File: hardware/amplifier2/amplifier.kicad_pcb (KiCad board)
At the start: 2 copper layers, 50 x 50 mm, 67 parts, among them IC1 AD8331, IC2 ISL55210, J1 0, P1 5V, P2 3V3, P3 Interface, T1 BALUN, T2 BALUN, U1 MCP4706/16/26, X1 IN_AD, X2 OUT_ISL_B, X3 OUT_AD_B, X4 OUT_AD, X5 IN_ISL, X6 OUT_ISL

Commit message: rerouting nearly done; added remaining footprints
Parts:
- added C26: 82p, Capacitors_SMD:C_0603, F.Cu at (54.4, 168.4)
- added C27: 100u, Capacitors_SMD:C_0603, F.Cu at (234.7, 165.5)
- added C28: 10n, Capacitors_SMD:C_0603, F.Cu at (228.0, 166.8)
- added C29: 180p, Capacitors_SMD:C_0603, F.Cu at (62.8, 166.5)
- added C30: 180p, Capacitors_SMD:C_0603, F.Cu at (70.8, 154.6)
- added C31: 180p, Capacitors_SMD:C_0603, F.Cu at (53.8, 152.0)
- added C32: 100n, Capacitors_SMD:C_0603, F.Cu at (98.8, 168.5)
- added C33: 82p, Capacitors_SMD:C_0603, F.Cu at (51.5, 159.7)
- added C34: 100n, Capacitors_SMD:C_0603, F.Cu at (95.6, 169.1)
- added C35: 100n, Capacitors_SMD:C_0603, F.Cu at (89.2, 157.9)
- added C36: 100n, Capacitors_SMD:C_0603, F.Cu at (81.7, 156.7)
- added C37: 100n, Capacitors_SMD:C_0603, F.Cu at (84.5, 164.7)
- added C38: 100n, Capacitors_SMD:C_0603, F.Cu at (96.6, 148.4)
- added C39: 100n, Capacitors_SMD:C_0603, F.Cu at (96.6, 149.9)
- added C40: 22p, Capacitors_SMD:C_0603, F.Cu at (94.4, 149.2)
- added C41: 10p, Capacitors_SMD:C_0603, F.Cu at (87.1, 152.2)
- added C42: TBD, Capacitors_SMD:C_0603, F.Cu at (110.7, 174.3)
- added C43: 100n, Capacitors_SMD:C_0603, F.Cu at (92.0, 155.2)
- added C44: 2u2, Capacitors_SMD:C_0603, F.Cu at (90.7, 159.3)
- added C45: 1u, Capacitors_SMD:C_0603, F.Cu at (84.7, 153.0)
- added C46: 100n, Capacitors_SMD:C_0402, F.Cu at (84.3, 156.7)
- added C47: 2u2, Capacitors_SMD:C_0603, F.Cu at (84.0, 155.2)
- added C48: 1u, Capacitors_SMD:C_0603, F.Cu at (83.2, 153.0)
- added D1: LED, LEDs:LED_0603, F.Cu at (53.2, 180.6)
- added D2: LED, LEDs:LED_0603, F.Cu at (53.2, 178.9)
- added IC4: NC7SVU04, SDRfootprints:SOT353, F.Cu at (94.9, 165.3)
- added IC5: LTC2252, Housings_DFN_QFN:QFN-32-1EP_5x5mm_Pitch0.5mm, F.Cu at (84.5, 160.4)
- added JP1: DE0_nano_GPIO-1, Pin_Headers:Pin_Header_Angled_2x20, F.Cu at (108.6, 178.4)
- added L10: 307n, SDRfootprints:Coil_132-XXSM_L_, F.Cu at (56.7, 154.0)
- added L11: 390n, SDRfootprints:1008, F.Cu at (91.2, 147.8)
- added L12: 390n, SDRfootprints:1008, F.Cu at (91.2, 150.4)
- added L7: 307n, SDRfootprints:Coil_132-XXSM_L_, F.Cu at (51.4, 166.4)
- added L8: 380n, SDRfootprints:Coil_132-XXSM_L_, F.Cu at (62.1, 162.8)
- added L9: 380n, SDRfootprints:Coil_132-XXSM_L_, F.Cu at (67.4, 150.4)
- added P4: VGA - LNA, Connect:bornier4, F.Cu at (62.7, 107.3)
- added P5: LNA - SDR, Connect:bornier4, F.Cu at (113.0, 142.5)
- added R19: 10k, Resistors_SMD:R_0603, F.Cu at (98.8, 160.2)
- added R20: 10k, Resistors_SMD:R_0603, F.Cu at (97.3, 158.4)
- added R21: 23k2, Resistors_SMD:R_0603, F.Cu at (240.3, 165.6)
- added R22: 13k3, Resistors_SMD:R_0603, F.Cu at (247.8, 163.1)
- added R23: 470, Resistors_SMD:R_0603, F.Cu at (56.0, 180.6)
- added R24: 470, Resistors_SMD:R_0603, F.Cu at (56.0, 178.9)
- added R25: 10k, Resistors_SMD:R_0603, F.Cu at (108.2, 173.5)
- added R26: 3k9, Resistors_SMD:R_0603, F.Cu at (87.1, 153.8)
- added R27: 100, Resistors_SMD:R_0603, F.Cu at (91.3, 153.0)
- added R28: 100, Resistors_SMD:R_0603, F.Cu at (89.6, 153.0)
- added R29: 10k, Resistors_SMD:R_0603, F.Cu at (91.6, 164.2)
- added R30: 22k, Resistors_SMD:R_0603, F.Cu at (91.6, 162.6)
- added R31: 22R, Resistors_SMD:R_0603, F.Cu at (86.3, 155.9)
- added R32: 0R, Resistors_SMD:R_0603, F.Cu at (89.6, 155.9)
- added R33: 22R, Resistors_SMD:R_0603, F.Cu at (88.0, 155.9)
- added R34: 0R, Resistors_SMD:R_0603, F.Cu at (91.0, 160.9)
- added R35: TBD, Resistors_SMD:R_0603, F.Cu at (101.4, 154.7)
- added R36: TBD, Resistors_SMD:R_0603, F.Cu at (104.0, 154.7)
- added R37: TBD, Resistors_SMD:R_0603, F.Cu at (83.8, 130.4)
- added R38: TBD, Resistors_SMD:R_0603, F.Cu at (82.0, 130.4)
- added RP1: R_PACK8, SDRfootprints:2406, F.Cu at (83.7, 166.9)
- added RP2: R_PACK8, SDRfootprints:2406, F.Cu at (90.8, 166.9)
- added SW1: SW_PUSH, Buttons_Switches_SMD:SW_SPST_PTS645, F.Cu at (115.6, 177.5)
- added T3: BALUN, SDRfootprints:CX2041NLT, F.Cu at (102.7, 159.6)
- added T4: BALUN, SDRfootprints:CX2041NLT, F.Cu at (83.0, 125.9)
- added W4: CLCK EXT, Measurement_Points:Test_Point_Keystone_5005-5009_Compact, F.Cu at (158.6, 182.3)
- added X7: OUT_AD, SDRfootprints:1-1337543-0, F.Cu at (44.1, 117.5)
- added Y1: FVXO-HC53BR, SDRfootprints:OSC_631-1265-1-ND, F.Cu at (99.6, 162.9)
- P1: footprint Pin_Headers:Pin_Header_Angled_1x02 -> Connect:bornier2
- P2: value 3V3 -> UART; footprint Pin_Headers:Pin_Header_Angled_1x02 -> Connectors_Molex:Molex_PicoBlade_53398-0471_04x1.25mm_Straight
- P3: value Interface -> DAC Interface
- X2: value OUT_ISL_B -> IN_FILTER
- X3: value OUT_AD_B -> OUT_FILTER
- X4: value OUT_AD -> IN_ADC
- moved P1 184.8 mm to (255.3, 168.0)
- moved P2 183.8 mm to (44.2, 181.9), turned to 0 degrees
- moved C13 138.6 mm to (223.0, 152.2)
- moved C15 138.6 mm to (229.5, 152.3)
- moved C17 138.6 mm to (235.6, 152.2)
- moved C20 138.6 mm to (242.3, 152.2)
- moved L3 138.6 mm to (226.3, 150.7)
- moved L4 138.6 mm to (238.9, 150.7)
- moved X3 126.9 mm to (44.1, 155.8), turned to 90 degrees
- moved X2 125.1 mm to (44.1, 171.8)
- moved T2 96.1 mm to (48.9, 116.3), turned to 270 degrees
- moved L5 92.2 mm to (89.0, 137.9), turned to 0 degrees
- moved R7 90.0 mm to (52.9, 120.7), turned to 0 degrees
- moved R9 89.4 mm to (91.3, 137.4), turned to 90 degrees
- moved R11 89.4 mm to (86.4, 134.6), turned to 270 degrees
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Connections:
- P2 pad 1: GNDA -> +3V3
- P2 pad 2: +3V3 -> /RX
- R17 pad 1: /OUT2+ -> /OUT2-
- R18 pad 1: /OUT2- -> /OUT2+
- X2 pad 1: Net-(T1-Pad1) -> Net-(C26-Pad1)
- X3 pad 1: Net-(T2-Pad1) -> Net-(C33-Pad1)
- X4 pad 1: /OUT2+ -> Net-(T3-Pad1)
- X4 pad 2: /OUT2- -> GNDA
- X5 pad 1: /IN2+ -> Net-(T4-Pad1)
- X5 pad 2: /IN2- -> GNDA
- X6 pad 1: /OUT1+ -> Net-(T1-Pad1)
- X6 pad 2: /OUT1- -> GNDA
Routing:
- net /SW1: track 0.00 -> 27.7 mm
- net /IN3-: track 0.00 -> 23.6 mm
- net /CLK: track 0.00 -> 22.3 mm
- net /RX: track 0.00 -> 21.6 mm
- net /TX: track 0.00 -> 21.1 mm
- net /IN3+: track 0.00 -> 20.8 mm, vias 0 -> 1
- net /D12: track 0.00 -> 18.9 mm
- net /OUT2-: track 0.01 -> 17.7 mm
- net /D11: track 0.00 -> 16.1 mm
- net /HILO: track 15.9 -> 0.00 mm
- net /OUT2+: track 0.00 -> 15.2 mm, vias 0 -> 1
- net /D0: track 0.00 -> 15.0 mm
- net /D9: track 0.00 -> 14.6 mm
- net Net-(C41-Pad1): track 0.00 -> 14.5 mm
- net /D1: track 0.00 -> 14.3 mm
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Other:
- board outline removed

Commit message: last state; minor changes still to do; powersupply missing; outline missing
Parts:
- removed W4: CLCK EXT, Measurement_Points:Test_Point_Keystone_5005-5009_Compact
- moved P3 47.3 mm to (135.2, 146.7)
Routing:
- net /HILO: track 0.00 -> 97.0 mm, vias 0 -> 1
- net /SDA: track 8.34 -> 97.5 mm, vias 0 -> 1
- net /SCL: track 10.4 -> 90.6 mm, vias 0 -> 1
- net /OUT1-: track 6.86 -> 26.1 mm
- net /OUT1+: track 3.85 -> 22.5 mm
- net (no net): track 12.3 -> 2.47 mm, vias 4 -> 3
- net Net-(T1-Pad1): track 4.05 -> 8.11 mm
- net +3V3: track 15.8 -> 19.6 mm
- net +3.3VADC: track 7.86 -> 7.05 mm

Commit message: all routing but PSU done; maybe schema needs nicer annotations
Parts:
- removed P3: DAC Interface, Pin_Headers:Pin_Header_Angled_1x03
- P1: footprint Connect:bornier2 -> SDRfootprints:ED365-2
- P4, P5: footprint Connect:bornier4 -> SDRfootprints:ED365-4
- moved P1 183.7 mm to (82.0, 107.3), turned to 180 degrees
- moved R22 172.4 mm to (79.1, 127.8)
- moved R21 162.6 mm to (82.2, 127.8)
- moved C27 160.4 mm to (77.2, 135.2)
- moved C15 157.7 mm to (72.2, 141.8), turned to 0 degrees
- moved C20 154.8 mm to (88.0, 139.6), turned to 180 degrees
- moved C17 153.0 mm to (82.9, 141.5), turned to 90 degrees
- moved L3 153.0 mm to (73.8, 138.7), turned to 180 degrees
- moved L4 152.6 mm to (86.5, 143.0), turned to 0 degrees
- moved C13 151.7 mm to (72.3, 135.3), turned to 180 degrees
- moved C28 149.4 mm to (82.9, 131.5)
- moved L5 15.1 mm to (103.1, 132.6)
- moved C23 15.1 mm to (102.8, 125.1)
- moved C25 15.1 mm to (108.2, 125.5)
- moved IC2 15.1 mm to (102.6, 127.2)
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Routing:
- net +5V: track 3.30 -> 97.5 mm, vias 0 -> 1
- net +3V3: track 19.6 -> 103.0 mm, vias 0 -> 4
- net +3.3VADC: track 7.05 -> 87.4 mm, vias 0 -> 5
- net /IN2-: track 7.76 -> 51.9 mm, vias 0 -> 1
- net /IN2+: track 5.71 -> 45.8 mm, vias 0 -> 1
- net +5VA: track 35.8 -> 55.9 mm, vias 2 -> 6
- net /OUT1+: track 22.5 -> 12.8 mm
- net /OUT1-: track 26.1 -> 18.8 mm
- net /IN3-: track 23.6 -> 30.3 mm
- net /IN3+: track 20.8 -> 27.3 mm
- net GNDA: track 116.4 -> 111.2 mm, vias 71 -> 60
- net /OUT2+: track 15.2 -> 18.7 mm
- net Net-(T3-Pad1): track 10.8 -> 13.7 mm
- net (no net): track 2.47 -> 0.00 mm, vias 3 -> 0
- net Net-(C30-Pad1): track 9.93 -> 12.4 mm
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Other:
- board outline added: 92 x 82 mm
- board text added: "ADC"
- board text added: "LGA"
- board text added: "LP"
- board text added: "PSU"
- board text added: "VGA"

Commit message: Updated and placed LDO, added wip bom. routing is wip
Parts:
- added IC3: LP38798, Housings_DFN_QFN:DFN-12-1EP_4x4mm_Pitch0.5mm, F.Cu at (82.9, 135.6)
- C27: footprint Capacitors_SMD:C_0603 -> Capacitors_SMD:C_1206
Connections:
- IC2 pad 10: Net-(IC2-Pad10) -> (no net)
- IC2 pad 11: Net-(IC2-Pad11) -> (no net)
- IC4 pad 1: Net-(IC4-Pad1) -> (no net)
- IC5 pad 9: Net-(IC5-Pad9) -> (no net)
- JP1 pad 15: Net-(JP1-Pad15) -> (no net)
- JP1 pad 18: Net-(JP1-Pad18) -> (no net)
- JP1 pad 2: Net-(JP1-Pad2) -> (no net)
- JP1 pad 20: Net-(JP1-Pad20) -> (no net)
- JP1 pad 25: Net-(JP1-Pad25) -> (no net)
- JP1 pad 27: Net-(JP1-Pad27) -> (no net)
- JP1 pad 3: Net-(JP1-Pad3) -> (no net)
- JP1 pad 32: Net-(JP1-Pad32) -> (no net)
- JP1 pad 33: Net-(JP1-Pad33) -> (no net)
- JP1 pad 34: Net-(JP1-Pad34) -> (no net)
- JP1 pad 35: Net-(JP1-Pad35) -> (no net)
- JP1 pad 8: Net-(JP1-Pad8) -> (no net)
- Y1 pad 5: Net-(Y1-Pad5) -> (no net)

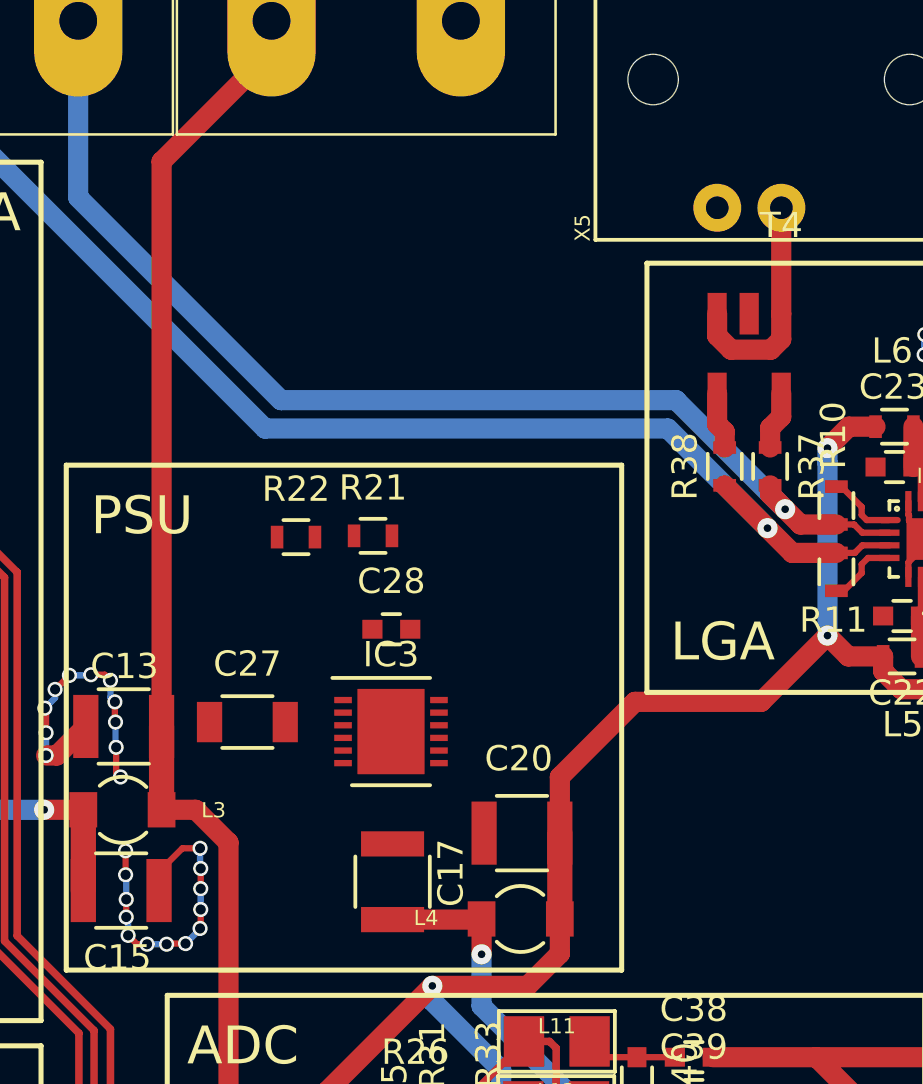
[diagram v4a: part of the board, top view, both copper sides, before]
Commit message: Routed LDO, updated LED resistors, added resistor part numbers
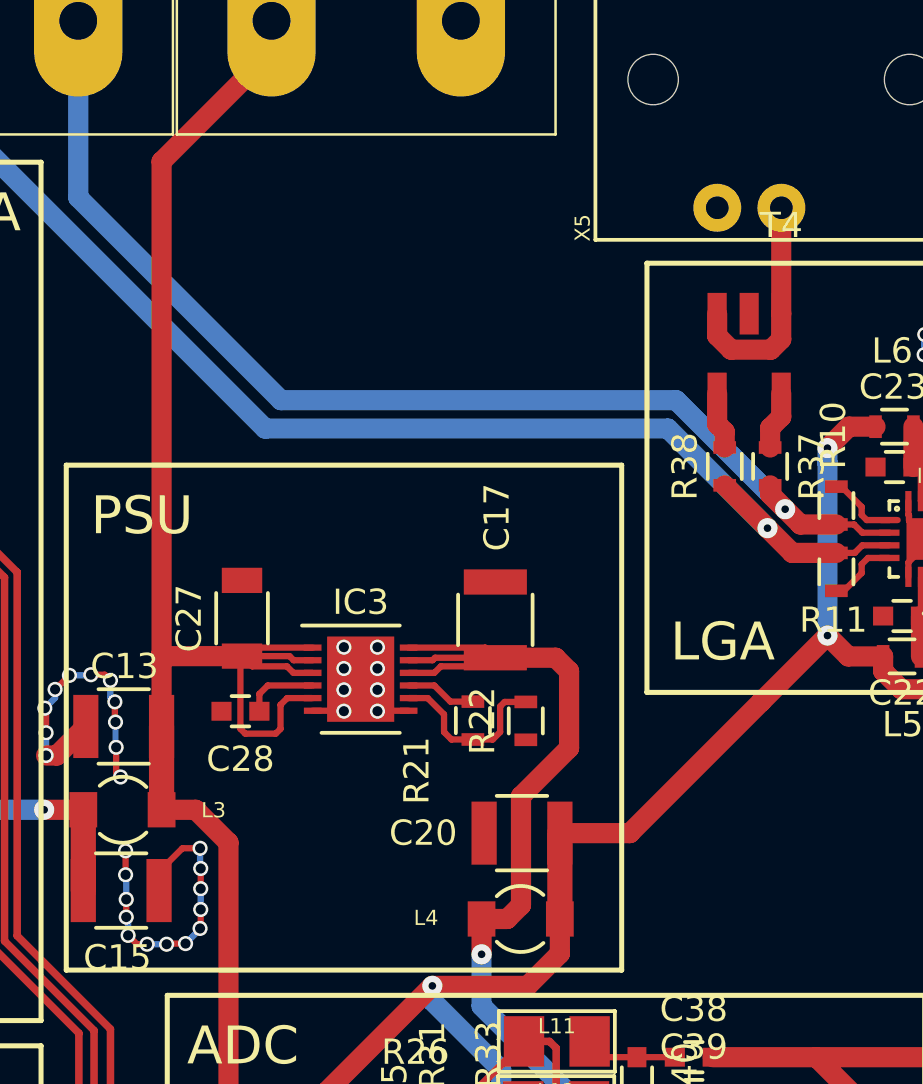
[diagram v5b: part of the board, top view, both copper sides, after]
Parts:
- moved R22 11.7 mm to (88.2, 135.1), turned to 90 degrees
- moved C17 11.1 mm to (87.0, 131.1)
- moved R21 8.32 mm to (86.1, 135.1), turned to 90 degrees
- moved C28 6.80 mm to (76.9, 134.7), turned to 180 degrees
- moved C27 4.12 mm to (77.0, 131.1), turned to 90 degrees
- moved IC3 2.40 mm to (81.7, 133.5)
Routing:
- net +3V3: track 103.0 -> 125.3 mm
- net +5V: track 97.5 -> 116.8 mm
- net Net-(IC3-Pad8): track 0.00 -> 6.94 mm
- net Net-(C28-Pad1): track 0.00 -> 2.94 mm
- net Net-(IC3-Pad9): track 0.00 -> 2.81 mm
- net GNDA: track 111.2 -> 113.7 mm, vias 60 -> 68
- net +3.3VADC: track 87.4 -> 86.1 mm

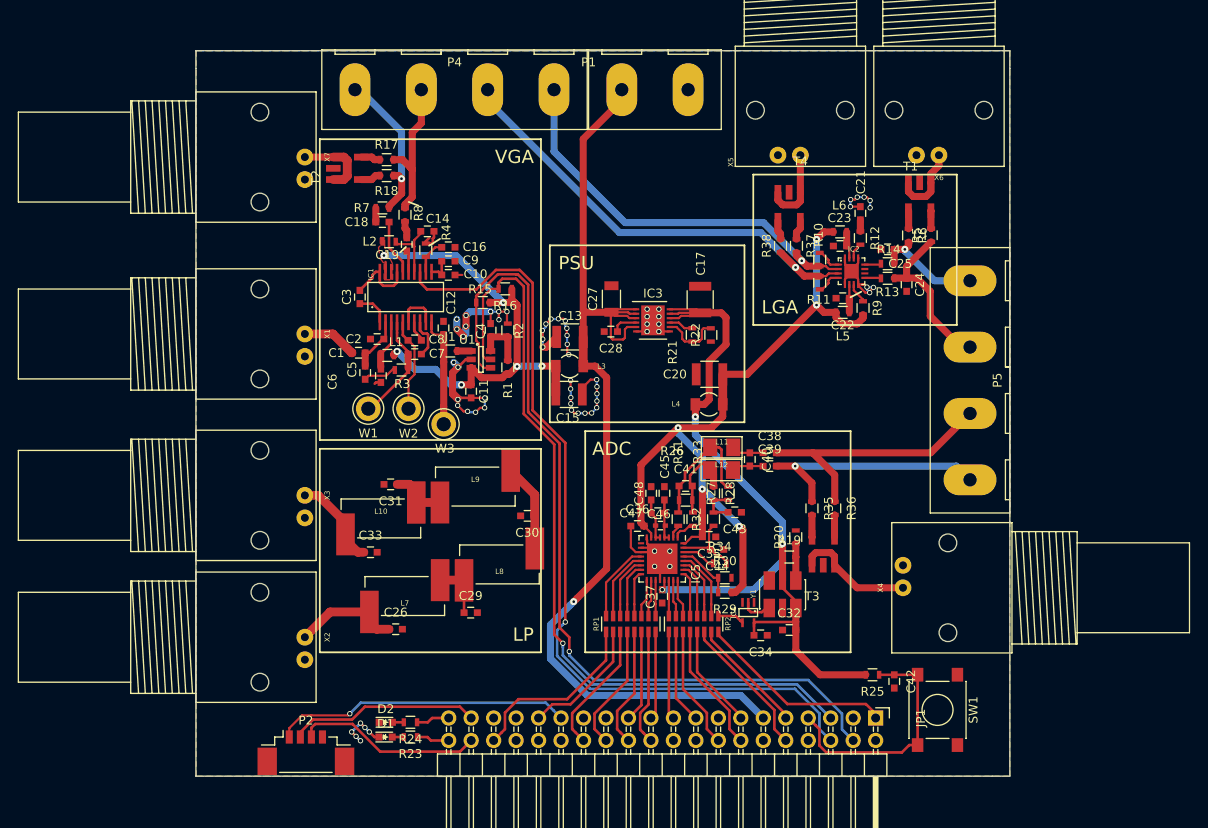
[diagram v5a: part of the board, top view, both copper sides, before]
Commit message: everything done routing; removed obsolete testpins; needs groundplane checks and stitchings; needs mounting holes; maybe elaborate in schema
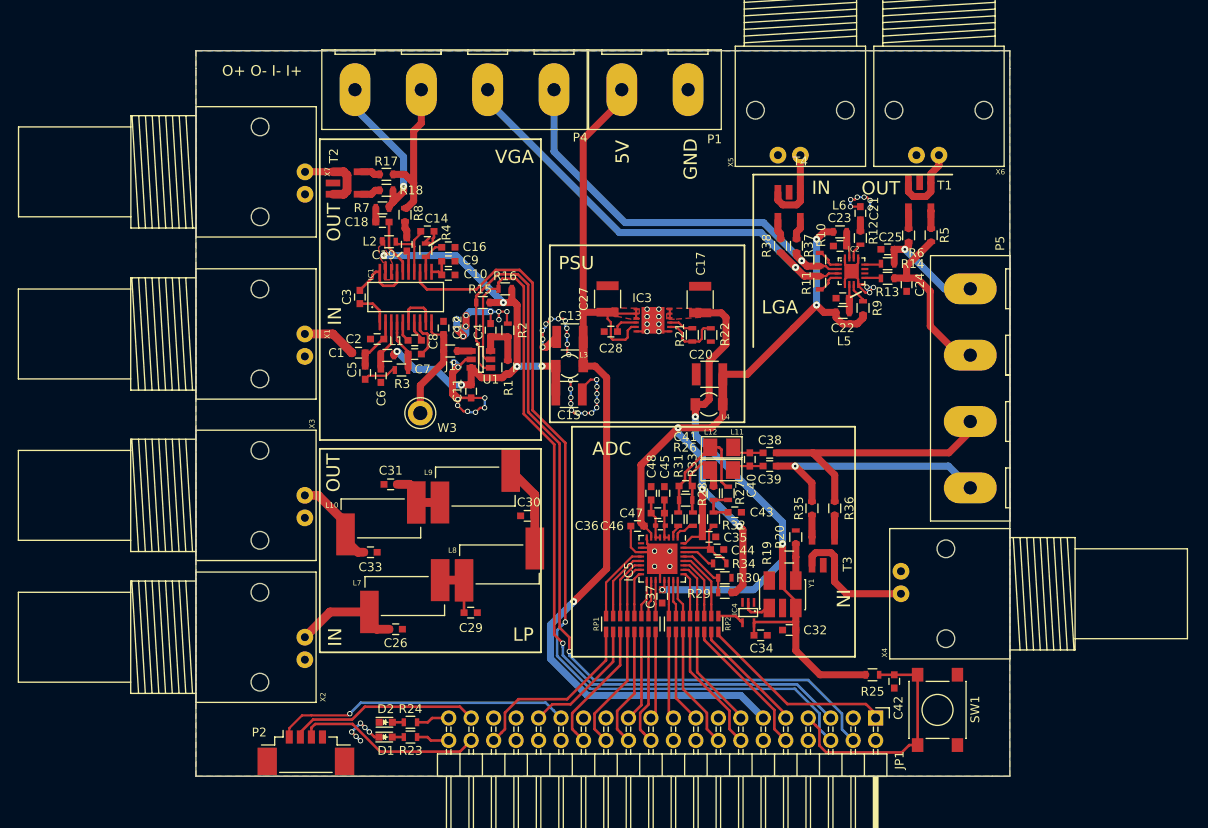
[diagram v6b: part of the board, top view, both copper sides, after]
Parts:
- removed W1, W2: TEST_1P, Measurement_Points:Test_Point_Keystone_5005-5009_Compact
- C27: footprint Capacitors_SMD:C_1206 -> Capacitors_SMD:C_1210
- IC3: footprint Housings_DFN_QFN:DFN-12-1EP_4x4mm_Pitch0.5mm -> SDRfootprints:WSON12
- R23, R24: value 470 -> 68
- moved W3 2.93 mm to (55.4, 144.0)
- moved X7 1.67 mm to (42.3, 119.2)
- moved R18 1.66 mm to (51.5, 118.8)
- moved R17 1.66 mm to (51.5, 117.0)
- moved T2 1.66 mm to (47.1, 118.0)
- moved P5 0.91 mm to (117.5, 141.2)
- moved X4 0.71 mm to (109.7, 161.8)
- moved C27 0.43 mm to (76.5, 131.1)
- turned IC3 to 90 degrees
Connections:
- IC2 pad 10: (no net) -> Net-(IC2-Pad10)
- IC2 pad 11: (no net) -> Net-(IC2-Pad11)
- IC4 pad 1: (no net) -> Net-(IC4-Pad1)
- IC5 pad 9: (no net) -> Net-(IC5-Pad9)
- JP1 pad 15: (no net) -> Net-(JP1-Pad15)
- JP1 pad 18: (no net) -> Net-(JP1-Pad18)
- JP1 pad 2: (no net) -> Net-(JP1-Pad2)
- JP1 pad 20: (no net) -> Net-(JP1-Pad20)
- JP1 pad 25: (no net) -> Net-(JP1-Pad25)
- JP1 pad 27: (no net) -> Net-(JP1-Pad27)
- JP1 pad 3: (no net) -> Net-(JP1-Pad3)
- JP1 pad 32: (no net) -> Net-(JP1-Pad32)
- JP1 pad 33: (no net) -> Net-(JP1-Pad33)
- JP1 pad 34: (no net) -> Net-(JP1-Pad34)
- JP1 pad 35: (no net) -> Net-(JP1-Pad35)
- JP1 pad 8: (no net) -> Net-(JP1-Pad8)
- Y1 pad 5: (no net) -> Net-(Y1-Pad5)
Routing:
- net +3V3: track 125.3 -> 116.6 mm
- net Net-(C8-Pad2): track 10.8 -> 2.46 mm
- net Net-(C7-Pad1): track 12.3 -> 6.12 mm
- net +5V: track 116.8 -> 111.6 mm
- net /OUT1-: track 18.8 -> 20.8 mm
- net GNDA: track 113.7 -> 112.1 mm
- net Net-(T3-Pad1): track 13.7 -> 14.8 mm
- added copper zone on F.Cu, net +3V3
- added copper zone on F.Cu, net +5V
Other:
- board text added: "5V"
- board text added: "GND"
- board text added: "IN"
- board text added: "O+ O- I- I+"
- board text added: "OUT"
